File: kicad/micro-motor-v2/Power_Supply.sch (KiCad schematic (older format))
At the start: 10 parts

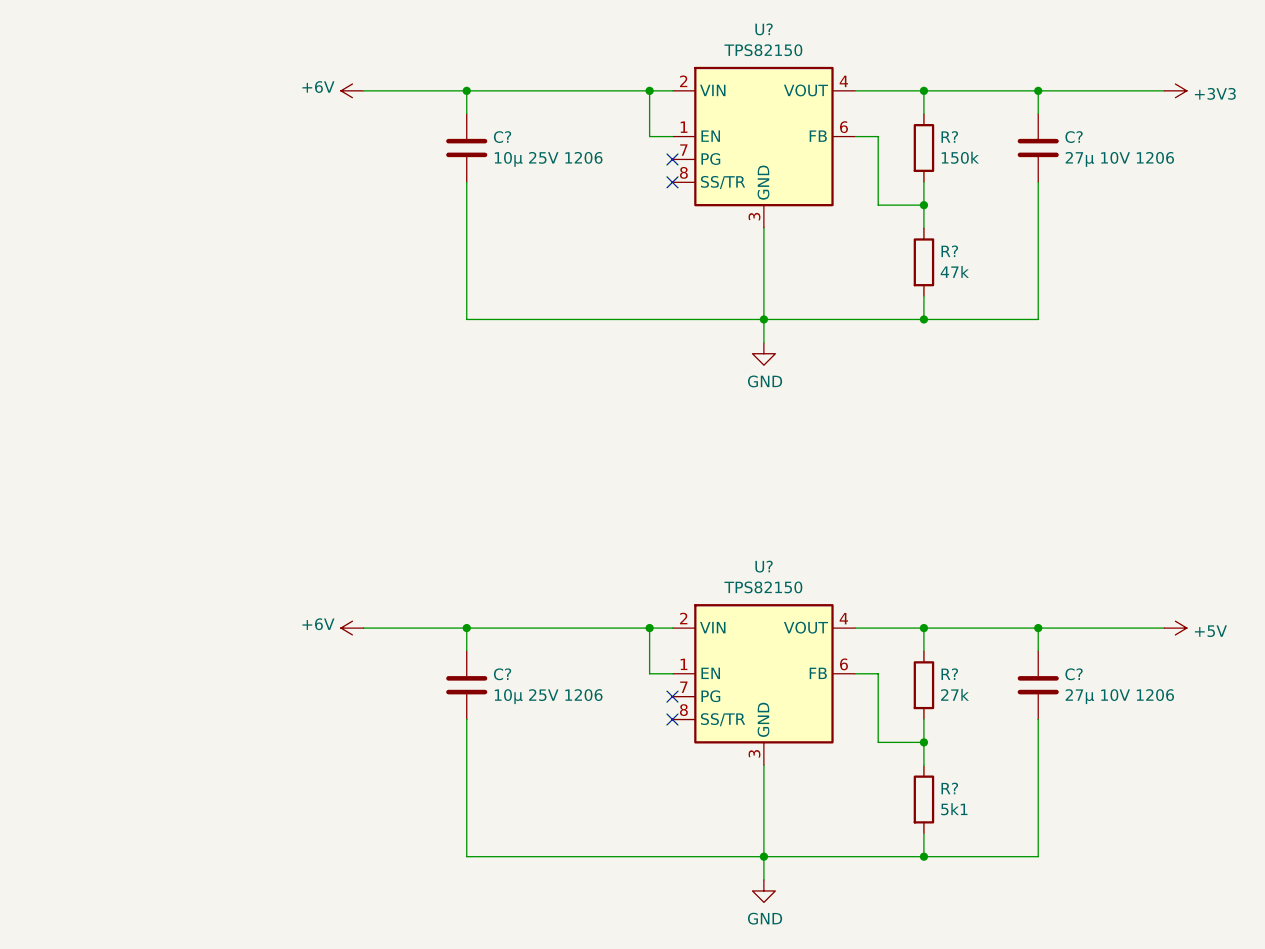
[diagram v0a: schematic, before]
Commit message: micro-motor-v2: Schematic finished
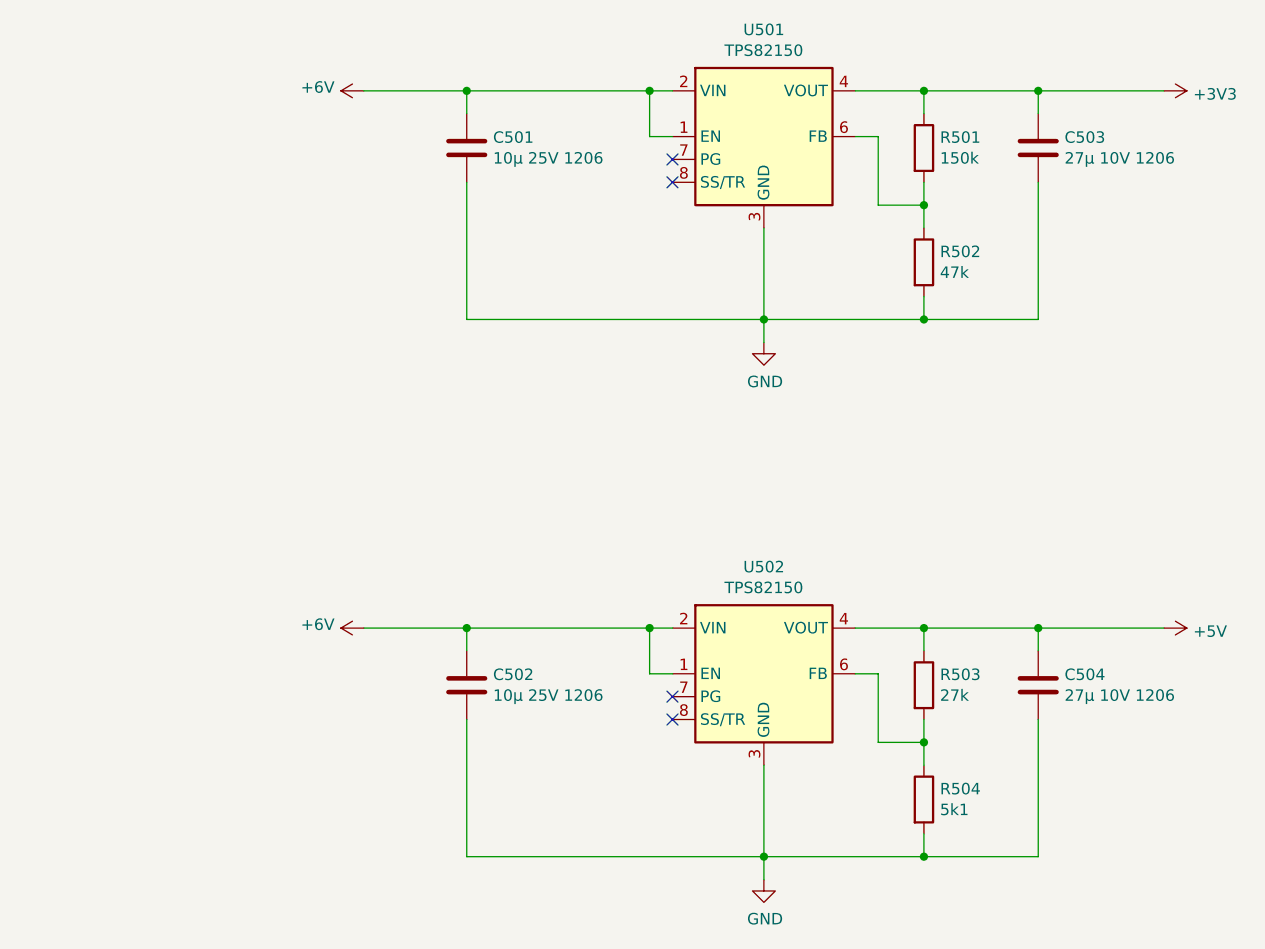
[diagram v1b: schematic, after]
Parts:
- C501, C502, C503, C504: renamed from C?; footprint (none) -> Capacitor_SMD:C_1206_3216Metric
- R501, R502, R503, R504: renamed from R?; footprint (none) -> Resistor_SMD:R_0402_1005Metric
- U501, U502: renamed from U?; footprint Package_LGA:Texas_MicroSiP-8-1EP_2.8x3.0mm_P0.65mm_EP1.1x1.9mm_SMD_ThermalVias -> Package_LGA:Texas_SIL0008D_MicroSiP-8-1EP_2.8x3mm_P0.65mm_EP1.1x1.9mm
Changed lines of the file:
@@
 $EndDescr
 $Comp
-L Regulator_Switching:TPS82150 U?
+L Regulator_Switching:TPS82150 U501
 U 1 1 5DDE5482
 P 5950 1900
-F 0 "U?" H 5950 2367 50  0000 C CNN
+F 0 "U501" H 5950 2367 50  0000 C CNN
 F 1 "TPS82150" H 5950 2276 50  0000 C CNN
-F 2 "Package_LGA:Texas_MicroSiP-8-1EP_2.8x3.0mm_P0.65mm_EP1.1x1.9mm_SMD_ThermalVias" H 5950 1250 50  0001 C CNN
+F 2 "Package_LGA:Texas_SIL0008D_MicroSiP-8-1EP_2.8x3mm_P0.65mm_EP1.1x1.9mm" H 5950 1250 50  0001 C CNN
 F 3 "http://www.ti.com/lit/ds/symlink/tps82150.pdf" H 5950 1150 50  0001 C CNN
 	1    5950 1900
@@
 $EndComp
 $Comp
-L Device:R R?
+L Device:R R501
 U 1 1 5DDE6A4B
 P 6650 1950
-F 0 "R?" H 6720 1996 50  0000 L CNN
+F 0 "R501" H 6720 1996 50  0000 L CNN
 F 1 "150k" H 6720 1905 50  0000 L CNN
-F 2 "" V 6580 1950 50  0001 C CNN
+F 2 "Resistor_SMD:R_0402_1005Metric" V 6580 1950 50  0001 C CNN
 F 3 "~" H 6650 1950 50  0001 C CNN
 	1    6650 1950
@@
 $EndComp
 $Comp
-L Device:R R?
+L Device:R R502
 U 1 1 5DDE7155
 P 6650 2450
-F 0 "R?" H 6720 2496 50  0000 L CNN
+F 0 "R502" H 6720 2496 50  0000 L CNN
 F 1 "47k" H 6720 2405 50  0000 L CNN
-F 2 "" V 6580 2450 50  0001 C CNN
+F 2 "Resistor_SMD:R_0402_1005Metric" V 6580 2450 50  0001 C CNN
 F 3 "~" H 6650 2450 50  0001 C CNN
 	1    6650 2450
@@
 $EndComp
 $Comp
-L Device:C C?
+L Device:C C503
 U 1 1 5DDE794A
 P 7150 1950
-F 0 "C?" H 7265 1996 50  0000 L CNN
+F 0 "C503" H 7265 1996 50  0000 L CNN
 F 1 "27µ 10V 1206" H 7265 1905 50  0000 L CNN
-F 2 "" H 7188 1800 50  0001 C CNN
+F 2 "Capacitor_SMD:C_1206_3216Metric" H 7188 1800 50  0001 C CNN
 F 3 "~" H 7150 1950 50  0001 C CNN
 	1    7150 1950
@@
 $EndComp
 $Comp
-L Device:C C?
+L Device:C C501
 U 1 1 5DDE7CAB
 P 4650 1950
-F 0 "C?" H 4765 1996 50  0000 L CNN
+F 0 "C501" H 4765 1996 50  0000 L CNN
 F 1 "10µ 25V 1206" H 4765 1905 50  0000 L CNN
-F 2 "" H 4688 1800 50  0001 C CNN
+F 2 "Capacitor_SMD:C_1206_3216Metric" H 4688 1800 50  0001 C CNN
 F 3 "~" H 4650 1950 50  0001 C CNN
 	1    4650 1950
@@
 Connection ~ 5950 2700
 $Comp
-L power:GND #PWR?
+L power:GND #PWR0503
 U 1 1 5DDE95B9
 P 5950 2800
-F 0 "#PWR?" H 5950 2550 50  0001 C CNN
+F 0 "#PWR0503" H 5950 2550 50  0001 C CNN
 F 1 "GND" H 5955 2627 50  0000 C CNN
 F 2 "" H 5950 2800 50  0001 C CNN
@@
 	5950 2800 5950 2700
 $Comp
-L power:+6V #PWR?
+L power:+6V #PWR0501
 U 1 1 5DDE9D9C
 P 4200 1700
-F 0 "#PWR?" H 4200 1550 50  0001 C CNN
+F 0 "#PWR0501" H 4200 1550 50  0001 C CNN
 F 1 "+6V" V 4215 1828 50  0000 L CNN
 F 2 "" H 4200 1700 50  0001 C CNN
@@
 $EndComp
 $Comp
-L Regulator_Switching:TPS82150 U?
+L Regulator_Switching:TPS82150 U502
 U 1 1 5DDEDF6B
 P 5950 4250
-F 0 "U?" H 5950 4717 50  0000 C CNN
+F 0 "U502" H 5950 4717 50  0000 C CNN
 F 1 "TPS82150" H 5950 4626 50  0000 C CNN
-F 2 "Package_LGA:Texas_MicroSiP-8-1EP_2.8x3.0mm_P0.65mm_EP1.1x1.9mm_SMD_ThermalVias" H 5950 3600 50  0001 C CNN
+F 2 "Package_LGA:Texas_SIL0008D_MicroSiP-8-1EP_2.8x3mm_P0.65mm_EP1.1x1.9mm" H 5950 3600 50  0001 C CNN
 F 3 "http://www.ti.com/lit/ds/symlink/tps82150.pdf" H 5950 3500 50  0001 C CNN
 	1    5950 4250
@@
 $EndComp
 $Comp
-L Device:R R?
+L Device:R R503
 U 1 1 5DDEDF75
 P 6650 4300
-F 0 "R?" H 6720 4346 50  0000 L CNN
+F 0 "R503" H 6720 4346 50  0000 L CNN
 F 1 "27k" H 6720 4255 50  0000 L CNN
-F 2 "" V 6580 4300 50  0001 C CNN
+F 2 "Resistor_SMD:R_0402_1005Metric" V 6580 4300 50  0001 C CNN
 F 3 "~" H 6650 4300 50  0001 C CNN
 	1    6650 4300
@@
 $EndComp
 $Comp
-L Device:R R?
+L Device:R R504
 U 1 1 5DDEDF7F
 P 6650 4800
-F 0 "R?" H 6720 4846 50  0000 L CNN
+F 0 "R504" H 6720 4846 50  0000 L CNN
 F 1 "5k1" H 6720 4755 50  0000 L CNN
-F 2 "" V 6580 4800 50  0001 C CNN
+F 2 "Resistor_SMD:R_0402_1005Metric" V 6580 4800 50  0001 C CNN
 F 3 "~" H 6650 4800 50  0001 C CNN
 	1    6650 4800
@@
 $EndComp
 $Comp
-L Device:C C?
+L Device:C C504
 U 1 1 5DDEDF89
 P 7150 4300
-F 0 "C?" H 7265 4346 50  0000 L CNN
+F 0 "C504" H 7265 4346 50  0000 L CNN
 F 1 "27µ 10V 1206" H 7265 4255 50  0000 L CNN
-F 2 "" H 7188 4150 50  0001 C CNN
+F 2 "Capacitor_SMD:C_1206_3216Metric" H 7188 4150 50  0001 C CNN
 F 3 "~" H 7150 4300 50  0001 C CNN
 	1    7150 4300
@@
 $EndComp
 $Comp
-L Device:C C?
+L Device:C C502
 U 1 1 5DDEDF93
 P 4650 4300
-F 0 "C?" H 4765 4346 50  0000 L CNN
+F 0 "C502" H 4765 4346 50  0000 L CNN
 F 1 "10µ 25V 1206" H 4765 4255 50  0000 L CNN
-F 2 "" H 4688 4150 50  0001 C CNN
+F 2 "Capacitor_SMD:C_1206_3216Metric" H 4688 4150 50  0001 C CNN
 F 3 "~" H 4650 4300 50  0001 C CNN
 	1    4650 4300
@@
 Connection ~ 5950 5050
 $Comp
-L power:GND #PWR?
+L power:GND #PWR0504
 U 1 1 5DDEDFBB
 P 5950 5150
-F 0 "#PWR?" H 5950 4900 50  0001 C CNN
+F 0 "#PWR0504" H 5950 4900 50  0001 C CNN
 F 1 "GND" H 5955 4977 50  0000 C CNN
 F 2 "" H 5950 5150 50  0001 C CNN
@@
 	5950 5150 5950 5050
 $Comp
-L power:+6V #PWR?
+L power:+6V #PWR0502
 U 1 1 5DDEDFC6
 P 4200 4050
-F 0 "#PWR?" H 4200 3900 50  0001 C CNN
+F 0 "#PWR0502" H 4200 3900 50  0001 C CNN
 F 1 "+6V" V 4215 4178 50  0000 L CNN
 F 2 "" H 4200 4050 50  0001 C CNN
@@
 $EndComp
 $Comp
-L power:+3V3 #PWR?
+L power:+3V3 #PWR0505
 U 1 1 5DDF5BFF
 P 7700 1700
-F 0 "#PWR?" H 7700 1550 50  0001 C CNN
+F 0 "#PWR0505" H 7700 1550 50  0001 C CNN
 F 1 "+3V3" V 7715 1828 50  0000 L CNN
 F 2 "" H 7700 1700 50  0001 C CNN
@@
 NoConn ~ 5550 4350
 $Comp
-L power:+5V #PWR?
+L power:+5V #PWR0506
 U 1 1 5DDF9E59
 P 7700 4050
-F 0 "#PWR?" H 7700 3900 50  0001 C CNN
+F 0 "#PWR0506" H 7700 3900 50  0001 C CNN
 F 1 "+5V" V 7715 4178 50  0000 L CNN
 F 2 "" H 7700 4050 50  0001 C CNN

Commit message: micro-motor-v2: layout: components placed
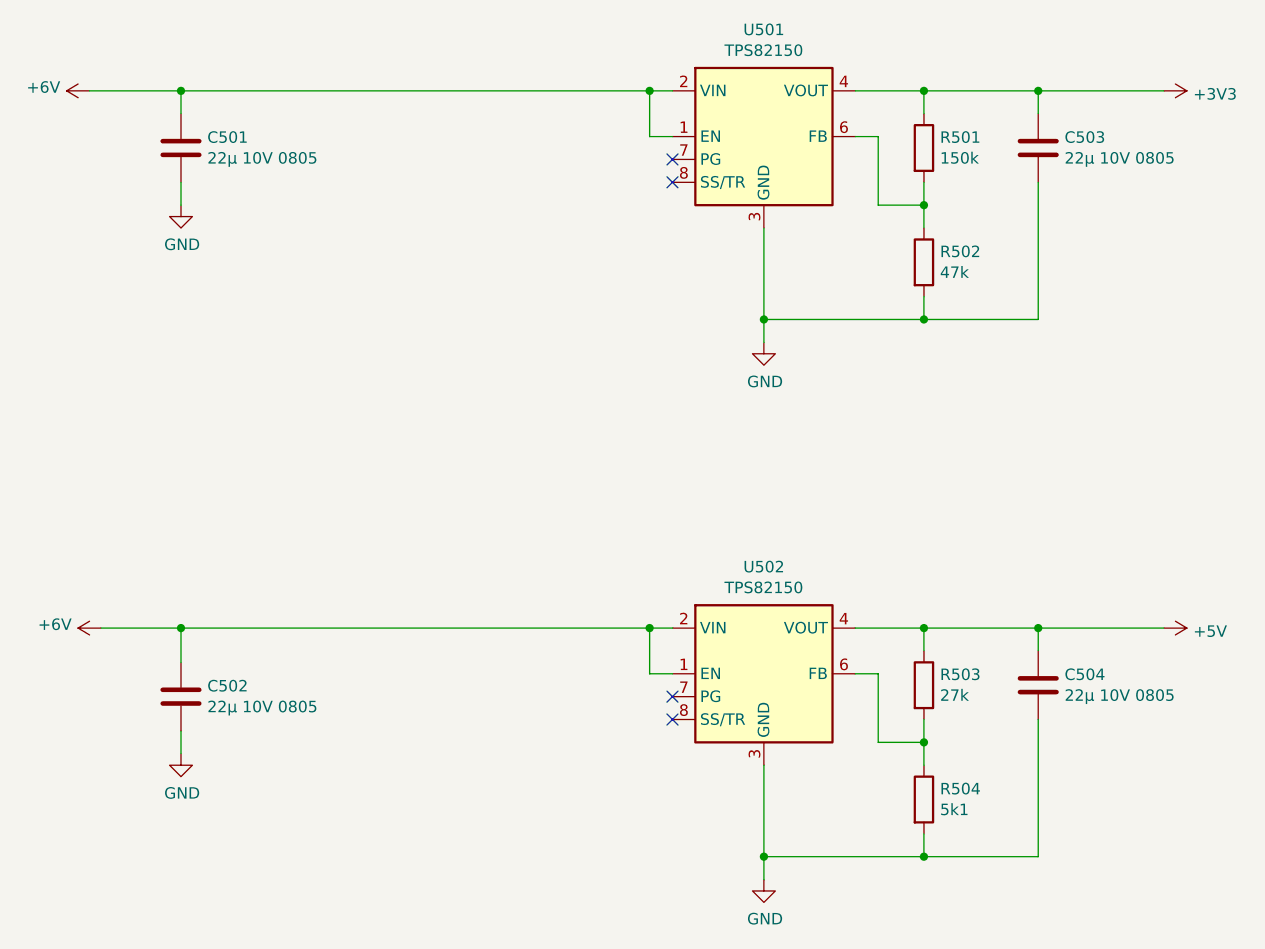
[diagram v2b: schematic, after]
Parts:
- C501, C502: value 10µ 25V 1206 -> 22µ 10V 0805; footprint Capacitor_SMD:C_1206_3216Metric -> Capacitor_SMD:C_0805_2012Metric
- C503, C504: value 27µ 10V 1206 -> 22µ 10V 0805; footprint Capacitor_SMD:C_1206_3216Metric -> Capacitor_SMD:C_0805_2012Metric
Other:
- moved on the sheet: C501
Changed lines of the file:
@@
 P 7150 1950
 F 0 "C503" H 7265 1996 50  0000 L CNN
-F 1 "27µ 10V 1206" H 7265 1905 50  0000 L CNN
-F 2 "Capacitor_SMD:C_1206_3216Metric" H 7188 1800 50  0001 C CNN
+F 1 "22µ 10V 0805" H 7265 1905 50  0000 L CNN
+F 2 "Capacitor_SMD:C_0805_2012Metric" H 7188 1800 50  0001 C CNN
 F 3 "~" H 7150 1950 50  0001 C CNN
 	1    7150 1950
@@
 L Device:C C501
 U 1 1 5DDE7CAB
-P 4650 1950
-F 0 "C501" H 4765 1996 50  0000 L CNN
-F 1 "10µ 25V 1206" H 4765 1905 50  0000 L CNN
-F 2 "Capacitor_SMD:C_1206_3216Metric" H 4688 1800 50  0001 C CNN
-F 3 "~" H 4650 1950 50  0001 C CNN
-	1    4650 1950
+P 3400 1950
+F 0 "C501" H 3515 1996 50  0000 L CNN
+F 1 "22µ 10V 0805" H 3515 1905 50  0000 L CNN
+F 2 "Capacitor_SMD:C_0805_2012Metric" H 3438 1800 50  0001 C CNN
+F 3 "~" H 3400 1950 50  0001 C CNN
+	1    3400 1950
 	1    0    0    -1
 $EndComp
@@
 Wire Wire Line
 	5450 1700 5550 1700
-Wire Wire Line
-	5450 1700 4650 1700
-Wire Wire Line
-	4650 1700 4650 1800
 Connection ~ 5450 1700
-Wire Wire Line
-	4650 1700 4200 1700
-Connection ~ 4650 1700
 Wire Wire Line
 	6350 1700 6650 1700
@@
 	7150 2700 7150 2100
 Connection ~ 6650 2700
-Wire Wire Line
-	5950 2700 4650 2700
-Wire Wire Line
-	4650 2700 4650 2100
 Connection ~ 5950 2700
 $Comp
@@
 L power:+6V #PWR0501
 U 1 1 5DDE9D9C
-P 4200 1700
-F 0 "#PWR0501" H 4200 1550 50  0001 C CNN
-F 1 "+6V" V 4215 1828 50  0000 L CNN
-F 2 "" H 4200 1700 50  0001 C CNN
-F 3 "" H 4200 1700 50  0001 C CNN
-	1    4200 1700
+P 3000 1700
+F 0 "#PWR0501" H 3000 1550 50  0001 C CNN
+F 1 "+6V" V 3015 1828 50  0000 L CNN
+F 2 "" H 3000 1700 50  0001 C CNN
+F 3 "" H 3000 1700 50  0001 C CNN
+	1    3000 1700
 	0    -1   -1   0
 $EndComp
@@
 P 7150 4300
 F 0 "C504" H 7265 4346 50  0000 L CNN
-F 1 "27µ 10V 1206" H 7265 4255 50  0000 L CNN
-F 2 "Capacitor_SMD:C_1206_3216Metric" H 7188 4150 50  0001 C CNN
+F 1 "22µ 10V 0805" H 7265 4255 50  0000 L CNN
+F 2 "Capacitor_SMD:C_0805_2012Metric" H 7188 4150 50  0001 C CNN
 F 3 "~" H 7150 4300 50  0001 C CNN
 	1    7150 4300
 	1    0    0    -1
 $EndComp
-$Comp
-L Device:C C502
-U 1 1 5DDEDF93
-P 4650 4300
-F 0 "C502" H 4765 4346 50  0000 L CNN
-F 1 "10µ 25V 1206" H 4765 4255 50  0000 L CNN
-F 2 "Capacitor_SMD:C_1206_3216Metric" H 4688 4150 50  0001 C CNN
-F 3 "~" H 4650 4300 50  0001 C CNN
-	1    4650 4300
-	1    0    0    -1
-$EndComp
 Wire Wire Line
 	5550 4250 5450 4250
@@
 Wire Wire Line
 	5450 4050 5550 4050
-Wire Wire Line
-	5450 4050 4650 4050
-Wire Wire Line
-	4650 4050 4650 4150
 Connection ~ 5450 4050
-Wire Wire Line
-	4650 4050 4200 4050
-Connection ~ 4650 4050
 Wire Wire Line
 	6350 4050 6650 4050
@@
 	7150 5050 7150 4450
 Connection ~ 6650 5050
-Wire Wire Line
-	5950 5050 4650 5050
-Wire Wire Line
-	4650 5050 4650 4450
 Connection ~ 5950 5050
 $Comp
@@
 Wire Wire Line
 	5950 5150 5950 5050
-$Comp
-L power:+6V #PWR0502
-U 1 1 5DDEDFC6
-P 4200 4050
-F 0 "#PWR0502" H 4200 3900 50  0001 C CNN
-F 1 "+6V" V 4215 4178 50  0000 L CNN
-F 2 "" H 4200 4050 50  0001 C CNN
-F 3 "" H 4200 4050 50  0001 C CNN
-	1    4200 4050
-	0    -1   -1   0
-$EndComp
 $Comp
 L power:+3V3 #PWR0505
@@
 	0    1    1    0
 $EndComp
+Wire Wire Line
+	3400 1800 3400 1700
+Connection ~ 3400 1700
+Wire Wire Line
+	3400 1700 3000 1700
+$Comp
+L power:GND #PWR0118
+U 1 1 5DB393BE
+P 3400 2200
+F 0 "#PWR0118" H 3400 1950 50  0001 C CNN
+F 1 "GND" H 3405 2027 50  0000 C CNN
+F 2 "" H 3400 2200 50  0001 C CNN
+F 3 "" H 3400 2200 50  0001 C CNN
+	1    3400 2200
+	1    0    0    -1
+$EndComp
+Wire Wire Line
+	3400 2200 3400 2100
+$Comp
+L Device:C C502
+U 1 1 5DBCABDE
+P 3400 4350
+F 0 "C502" H 3515 4396 50  0000 L CNN
+F 1 "22µ 10V 0805" H 3515 4305 50  0000 L CNN
+F 2 "Capacitor_SMD:C_0805_2012Metric" H 3438 4200 50  0001 C CNN
+F 3 "~" H 3400 4350 50  0001 C CNN
+	1    3400 4350
+	1    0    0    -1
+$EndComp
+$Comp
+L power:GND #PWR0507
+U 1 1 5DBCABE8
+P 3400 4600
+F 0 "#PWR0507" H 3400 4350 50  0001 C CNN
+F 1 "GND" H 3405 4427 50  0000 C CNN
+F 2 "" H 3400 4600 50  0001 C CNN
+F 3 "" H 3400 4600 50  0001 C CNN
+	1    3400 4600
+	1    0    0    -1
+$EndComp
+Wire Wire Line
+	3400 4600 3400 4500
+Wire Wire Line
+	3400 4200 3400 4050
+Wire Wire Line
+	3400 4050 5450 4050
+Wire Wire Line
+	3400 1700 5450 1700
+$Comp
+L power:+6V #PWR0502
+U 1 1 5DBD45BA
+P 3050 4050
+F 0 "#PWR0502" H 3050 3900 50  0001 C CNN
+F 1 "+6V" V 3065 4178 50  0000 L CNN
+F 2 "" H 3050 4050 50  0001 C CNN
+F 3 "" H 3050 4050 50  0001 C CNN
+	1    3050 4050
+	0    -1   -1   0
+$EndComp
+Wire Wire Line
+	3050 4050 3400 4050
+Connection ~ 3400 4050
 $EndSCHEMATC
